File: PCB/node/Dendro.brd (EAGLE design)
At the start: 59.7 x 47 mm, 6 parts

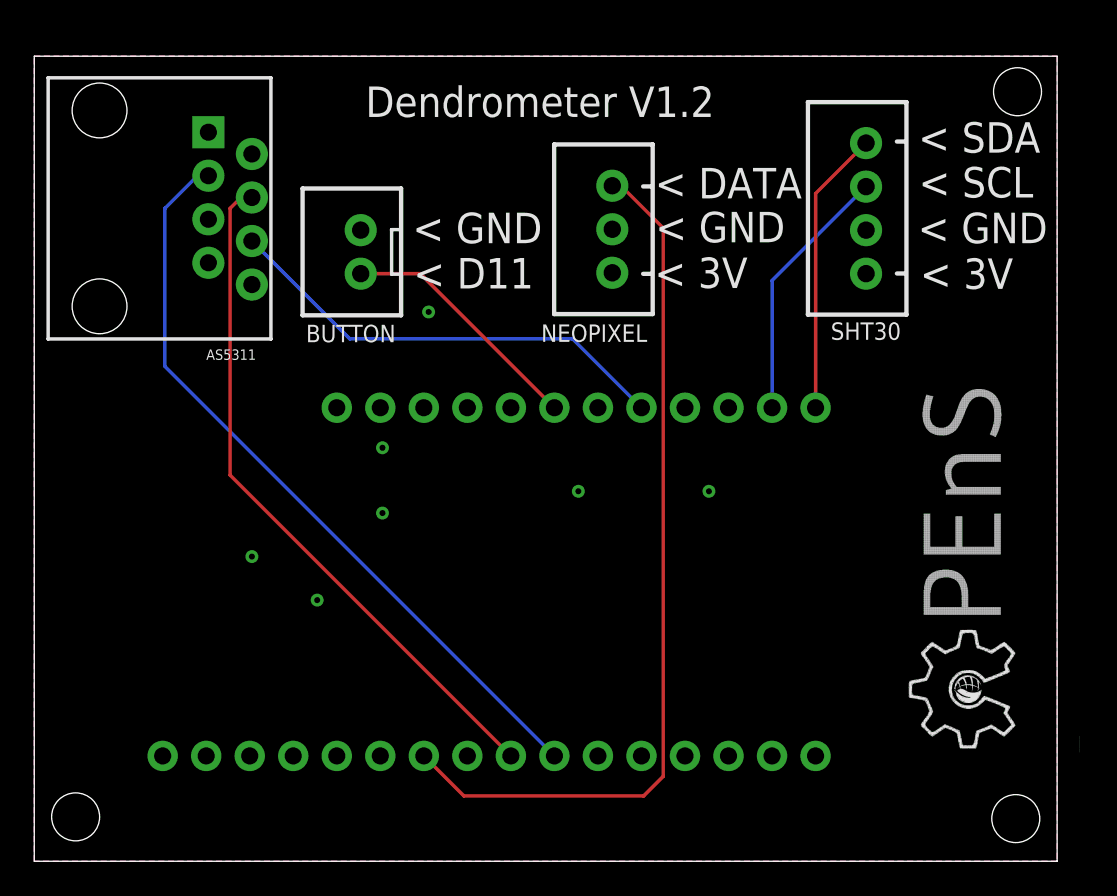
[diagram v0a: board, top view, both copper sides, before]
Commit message: Summer 2022 Deployment Prep
Updated PCBs and code, includes Loom V3 and HypnosV3.3 changes
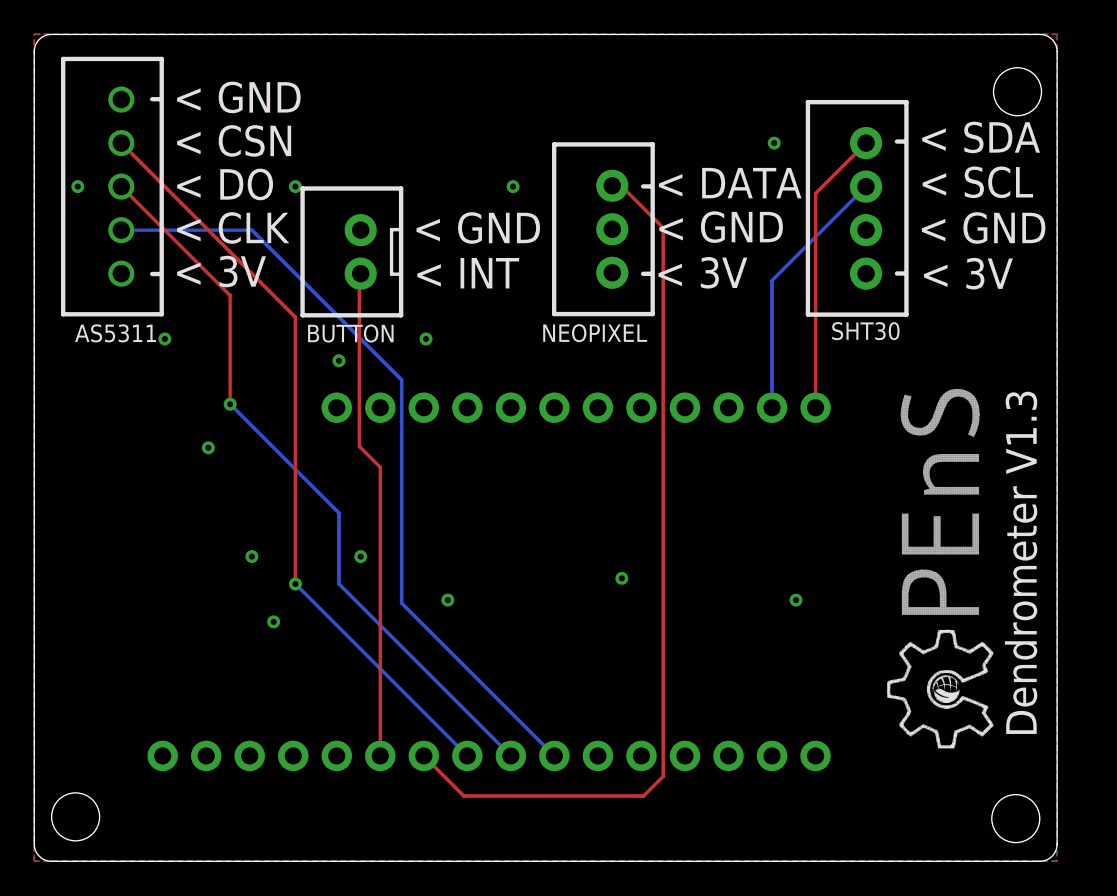
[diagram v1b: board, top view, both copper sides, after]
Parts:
- AS5311: value RJ45 -> JST-XH-05-PIN-ROUND-PAD; device SparkFun-Connectors:RJ45-8 -> Rembrandt Electronics - JST XH Connectors v1-0:JST-XH-05-PACKAGE-ROUND-PAD
- moved AS5311 1.80 mm to (5.08, 31.8), turned to 90 degrees
- moved U$1 1.27 mm to (59.7, -1.27)
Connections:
- net A2 renamed LED
- removed net D11: BUTTON.1, MS1.23
- new net INT: BUTTON.1, MS1.6
- net 3VRAIL: no longer AS5311.2
- net CSN: now also AS5311.4, MS1.8; no longer AS5311.6, MS1.21
- net DO: now also AS5311.3; no longer AS5311.4
- net SCLK: now also AS5311.2; no longer AS5311.3
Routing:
- net INT: track 0.00 -> 28.7 mm
- net CSN: track 26.8 -> 44.1 mm, vias 0 -> 1
- net D11: track 14.5 -> 0.00 mm
- net DO: track 40.3 -> 42.6 mm, vias 0 -> 1
- net SCLK: track 44.7 -> 45.6 mm
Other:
- board size 59.7 x 47 mm -> 59.7 x 48.2 mm
- board text added: "< CLK"
- board text added: "< CSN"
- board text added: "< DO"
- board text added: "< INT"
- board text added: "Dendrometer V1.3"
- board text removed: "< D11"
- board text removed: "Dendrometer V1.2"
